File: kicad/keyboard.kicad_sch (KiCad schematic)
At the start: 102 parts, among them SW1 SW_Push, SW10 SW_Push, SW11 SW_Push, SW12 SW_Push, SW13 SW_Push, SW14 SW_Push, SW15 SW_Push, SW16 SW_Push, SW17 SW_Push, SW18 SW_Push, SW19 SW_Push, SW2 SW_Push, SW20 SW_Push, SW21 SW_Push, SW22 SW_Push, SW23 SW_Push, SW24 SW_Push, SW25 SW_Push, SW26 SW_Push, SW27 SW_Push, SW28 SW_Push, SW29 SW_Push, SW3 SW_Push, SW30 SW_Push, SW31 SW_Push, SW32 SW_Push, SW33 SW_Push, SW34 SW_Push, SW35 SW_Push, SW36 SW_Push, SW37 SW_Push, SW38 SW_Push, SW39 SW_Push, SW4 SW_Push, SW40 SW_Push, SW41 SW_Push, SW42 SW_Push, SW43 SW_Push, SW44 SW_Push, SW45 SW_Push, SW46 SW_Push, SW47 SW_Push, SW48 SW_Push, SW5 SW_Push, SW6 SW_Push, SW7 SW_Push, SW8 SW_Push, SW9 SW_Push, U3 ATmega328-P, Y1 Crystal

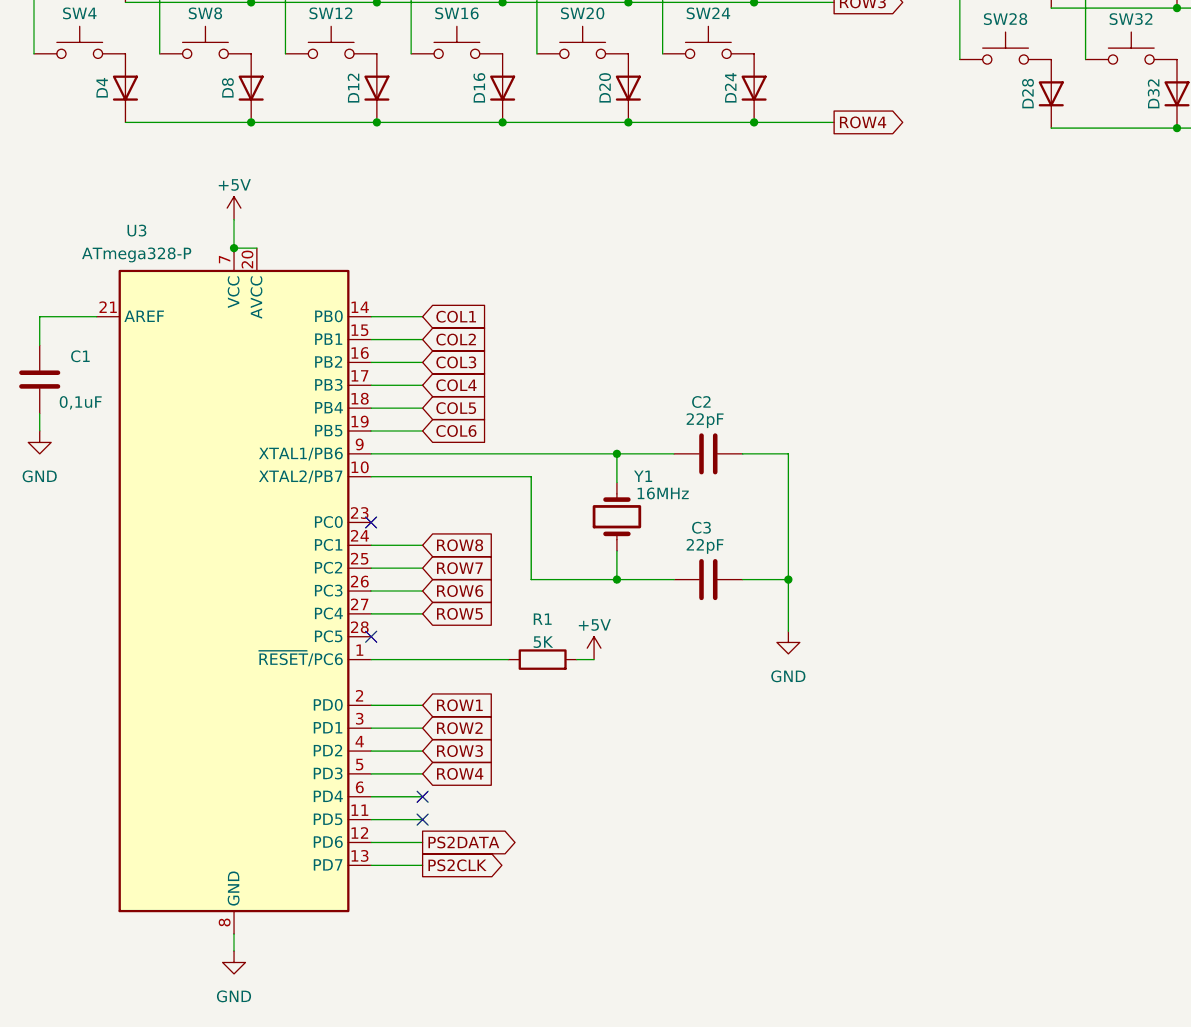
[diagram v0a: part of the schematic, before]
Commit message: WIP: v2.0 split board
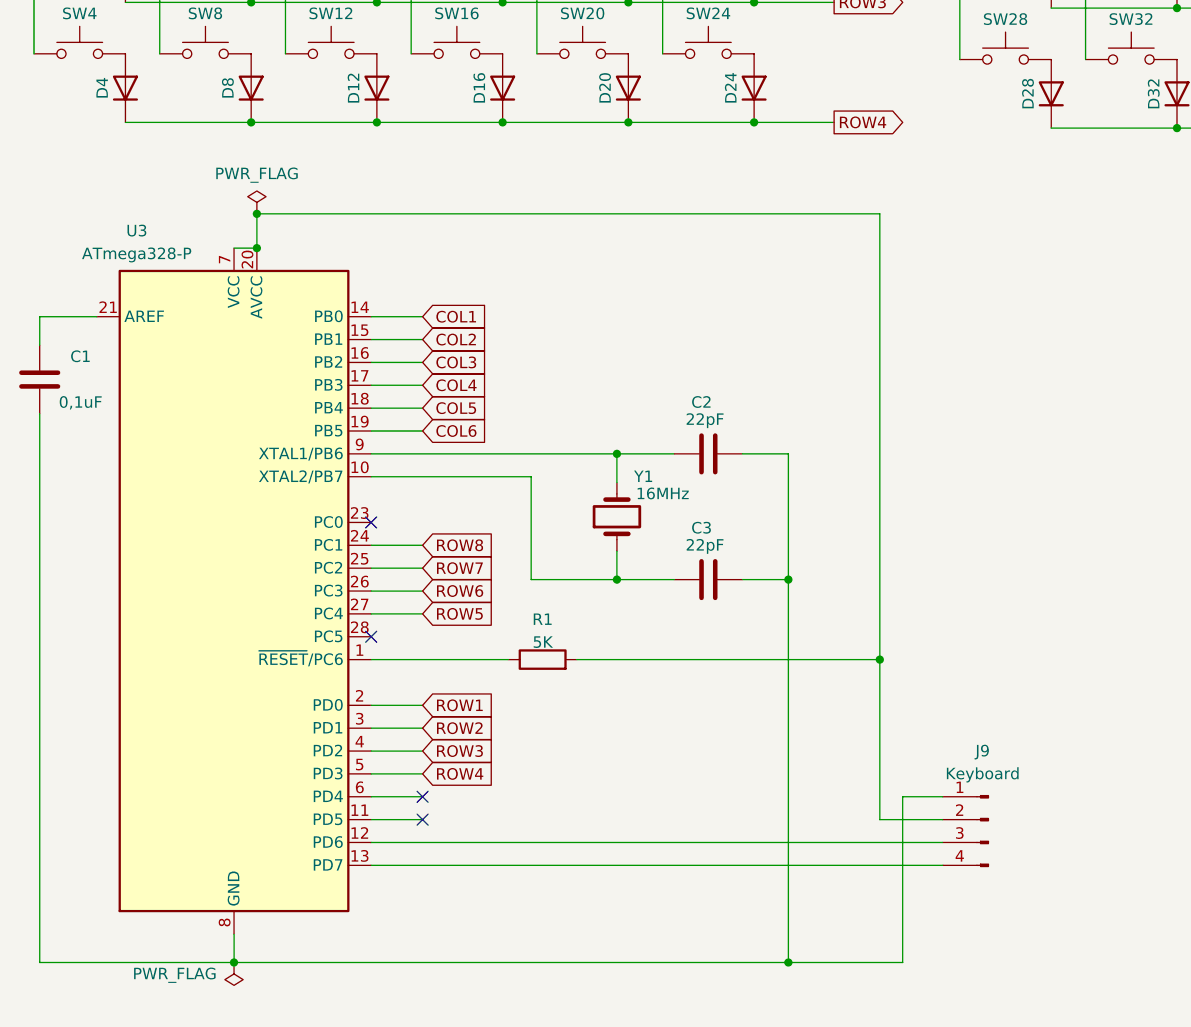
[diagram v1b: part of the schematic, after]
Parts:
- added J9: Keyboard, Connector_PinHeader_2.54mm:PinHeader_1x04_P2.54mm_Vertical, symbol Connector:Conn_01x04_Pin
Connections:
- net +5V: no longer names the net of R1.2, U3.20 (AVCC), U3.7 (VCC)
- net +5V: now also J9.2 (Pin_2)
- net GND: no longer names the net of C1.1, C2.1, C3.1, U3.22 (GND), U3.8 (GND)
- net GND: now also J9.1 (Pin_1)
- net PS2CLK: no longer names the net of U3.13 (PD7)
- net PS2CLK: now also J9.4 (Pin_4)
- net PS2DATA: no longer names the net of U3.12 (PD6)
- net PS2DATA: now also J9.3 (Pin_3)
